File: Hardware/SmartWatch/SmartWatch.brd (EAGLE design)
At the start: 36.8 x 40.6 mm, 70 parts, among them U1 STM32L476, U3 UG-2828GDEDF11, U4 FAN5331SX, U5 APDS-9960, U6 MCP73831, U7 AP2112K-3.3TRG-1

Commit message: finished schematic!
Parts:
- added R19, R22: 10k, resistor:R0603
- added R21: 10K, resistor:R0603
- moved U$41 18.3 mm to (11.5, 10.5), turned to 90 degrees
- moved C19 18.0 mm to (12.0, 8.00), turned to 0 degrees
- moved C18 17.5 mm to (25.0, 7.00), turned to 0 degrees
- moved U$39 16.7 mm to (25.0, 8.50), turned to 0 degrees
- moved U$5 4.92 mm to (9.50, 32.0)
- moved RN1 0.50 mm to (7.00, 20.5)
- moved U1 0.50 mm to (19.5, 14.5), turned to 135 degrees
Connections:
- removed net BT_IRQ: U2.8
- removed net MOSI/DATA1: U3.P$13
- removed net PA10: U1.43
- removed net PA13: U1.46
- removed net PA5: U1.21
- removed net PA6: U1.22
- removed net PA7: U1.23
- removed net PA8: U1.41
- removed net PB0: U1.26
- removed net PB1: U1.27
- removed net PB13: U1.34
- removed net PB14: U1.35
- removed net PB2: U1.28
- removed net PB8: U1.61
- removed net PB9: U1.62
- removed net PC10: U1.51
- removed net PC12: U1.53
- removed net PC4: U1.24
- removed net PC8: U1.39
- removed net PC9: U1.40
- removed net SCK/DATA0: U3.P$14
- new net BT_INT: U1.24, U2.8
- new net OLED_MOSI: U1.53, U3.P$13
- new net OLED_SCK: U1.51, U3.P$14
- net 3.3V: now also R21.2
- net BTN_BACK: now also U1.43
- net BTN_DN: now also U1.26
- net BTN_SEL: now also U1.27
- net BTN_UP: now also U1.28
- net BT_MISO: now also U1.22
- net BT_MOSI: now also U1.23
- net BT_SCK: now also U1.21
- net GND: now also R19.1, R22.1
- net G_INT: now also U1.39
- net IMU_INT: now also U1.40
- net IMU_NRESET: now also R22.2, U1.41
- net OLED_CS: now also R19.2
- net OLED_DC: now also U1.62
- net OLED_RES: now also U1.61
- net SCL: now also U1.34
- net SDA: now also U1.35
- net STAT: now also R21.1, U1.46
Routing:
- added copper zone on layer 1, net GND

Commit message: started board layout
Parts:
- added JP1: (no value), SparkFun-Connectors:1X02
- C1, C10, C11, C14, C2, C3, C4, C5, C6, C7, C8, C9: device microbuilder:0603-MINI -> resistor:C0603
- moved R2 47.7 mm to (18.0, 8.63), flipped to the bottom
- moved R21 46.1 mm to (3.67, 32.0), turned to 180 degrees
- moved R5 46.0 mm to (22.9, 8.89), flipped to the bottom
- moved C3 42.4 mm to (24.1, 8.89), flipped to the bottom
- moved C25 42.2 mm to (11.0, 17.1), turned to 135 degrees
- moved C28 40.0 mm to (11.9, 18.0), turned to 135 degrees
- moved C6 39.3 mm to (25.4, 8.89), flipped to the bottom, turned to 90 degrees
- moved R4 37.8 mm to (15.3, 8.63), flipped to the bottom
- moved C14 37.3 mm to (13.5, 8.68), flipped to the bottom
- moved D2 36.7 mm to (6.45, 29.3), flipped to the bottom
- moved C9 36.6 mm to (12.3, 8.68), flipped to the bottom
- moved C27 35.0 mm to (21.0, 24.1), turned to 90 degrees
- moved D3 33.9 mm to (21.4, 12.5), flipped to the bottom, turned to 90 degrees
- moved D1 33.5 mm to (23.1, 12.5), flipped to the bottom
- moved L1 29.1 mm to (7.08, 34.0), flipped to the bottom, turned to 270 degrees
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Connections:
- removed net 3.3V: BTN_BACK.3, BTN_BACK.4, BTN_BOOT0.3, BTN_BOOT0.4, BTN_DN.3, BTN_DN.4, BTN_NRST.3, BTN_NRST.4, BTN_SEL.3, BTN_SEL.4, BTN_UP.3, BTN_UP.4, C10.2, C11.2, C12.1, C13.1, C18.1, C19.1, C20.1, C21.1, C22.1, C23.1, C24.1, C25.1, C26.1, C29.1, C3.2, C5.2, C7.1, C9.2, L1.P$1, R21.2, R3.2, R8.2, R9.2, U$39.4, U$41.4, U$5.28, U$5.3, U$5.4, U1.1, U1.13, U1.19, U1.32, U1.48, U1.64, U3.P$27, U3.P$4, U4.4, U4.5, U5.5, U5.8, U7.5
- net +3V3: now also BTN_BACK.3, BTN_BACK.4, BTN_BOOT0.3, BTN_BOOT0.4, BTN_DN.3, BTN_DN.4, BTN_NRST.3, BTN_NRST.4, BTN_SEL.3, BTN_SEL.4, BTN_UP.3, BTN_UP.4, C10.2, C11.2, C12.1, C13.1, C18.1, C19.1, C20.1, C21.1, C22.1, C23.1, C24.1, C25.1, C26.1, C29.1, C3.2, C5.2, C7.1, C9.2, L1.P$1, R21.2, R3.2, R8.2, R9.2, U$39.4, U$41.4, U$5.28, U$5.3, U$5.4, U1.1, U1.13, U1.19, U1.32, U1.48, U1.64, U3.P$27, U3.P$4, U4.4, U4.5, U5.5, U5.8, U7.5
- net GND: now also JP1.1
- net VBAT: now also JP1.2
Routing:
- net +3V3: track 0.00 -> 35.0 mm
- net BTN_UP: track 0.00 -> 34.6 mm, vias 0 -> 1
- net BTN_NRST: track 0.00 -> 30.0 mm, vias 0 -> 1
- net BTN_DN: track 0.00 -> 29.5 mm, vias 0 -> 1
- net BTN_SEL: track 0.00 -> 21.3 mm, vias 0 -> 1
- net VUSB: track 0.00 -> 21.0 mm, vias 0 -> 1
- net BT_SCK: track 0.00 -> 17.2 mm, vias 0 -> 2
- net BT_MISO: track 0.00 -> 15.1 mm, vias 0 -> 2
- net D-: track 0.00 -> 13.6 mm, vias 0 -> 1
- net BT_MOSI: track 0.00 -> 13.1 mm, vias 0 -> 2
- net OLED_SCK: track 0.00 -> 12.2 mm, vias 0 -> 1
- net OLED_MOSI: track 0.00 -> 12.1 mm, vias 0 -> 1
- net VBAT: track 0.00 -> 11.3 mm
- net D+: track 0.00 -> 11.2 mm, vias 0 -> 1
- net BT_INT: track 0.00 -> 10.4 mm, vias 0 -> 2
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- added copper zone on layer 16, net GND

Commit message: finished PCB and added images
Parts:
- moved C2 41.1 mm to (26.7, 8.91), flipped to the bottom
- moved U4 41.0 mm to (33.3, 14.4)
- moved R6 38.8 mm to (34.6, 10.9), turned to 270 degrees
- moved R7 38.7 mm to (32.0, 10.9)
- moved C8 38.6 mm to (33.3, 10.9)
- moved C12 32.4 mm to (13.8, 34.0)
- moved C1 32.3 mm to (21.1, 31.8), turned to 270 degrees
- moved C7 31.7 mm to (28.3, 17.3), turned to 45 degrees
- moved D2 30.7 mm to (30.0, 9.60), flipped to the top
- moved R3 30.4 mm to (17.5, 24.0), turned to 0 degrees
- moved L1 30.1 mm to (30.0, 14.4), flipped to the top
- moved C4 28.9 mm to (10.6, 23.6), turned to 90 degrees
- moved R8 26.3 mm to (17.5, 22.8), turned to 0 degrees
- moved C5 25.3 mm to (7.83, 28.5), turned to 0 degrees
- moved R11 23.2 mm to (7.90, 25.8), turned to 0 degrees
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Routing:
- net +3V3: track 35.0 -> 263.1 mm, vias 0 -> 7
- net SDA: track 0.00 -> 30.2 mm, vias 0 -> 3
- net G_INT: track 0.00 -> 27.4 mm, vias 0 -> 2
- net STAT: track 3.87 -> 30.0 mm
- net BTN_BACK: track 4.94 -> 28.9 mm, vias 0 -> 1
- net SCL: track 0.00 -> 22.5 mm, vias 0 -> 2
- net BTN_BOOT0: track 4.98 -> 20.6 mm, vias 0 -> 1
- net 13V: track 0.00 -> 13.1 mm, vias 0 -> 1
- net IMU_NRESET: track 0.00 -> 9.75 mm
- net IMU_INT: track 0.00 -> 9.18 mm
- net N$5: track 0.00 -> 4.30 mm
- net N$8: track 0.00 -> 4.06 mm
- net N$4: track 0.00 -> 2.99 mm
- net VBAT: track 11.3 -> 13.9 mm
- net N$14: track 0.00 -> 2.11 mm
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- added copper zone on layer 1, net VUSB

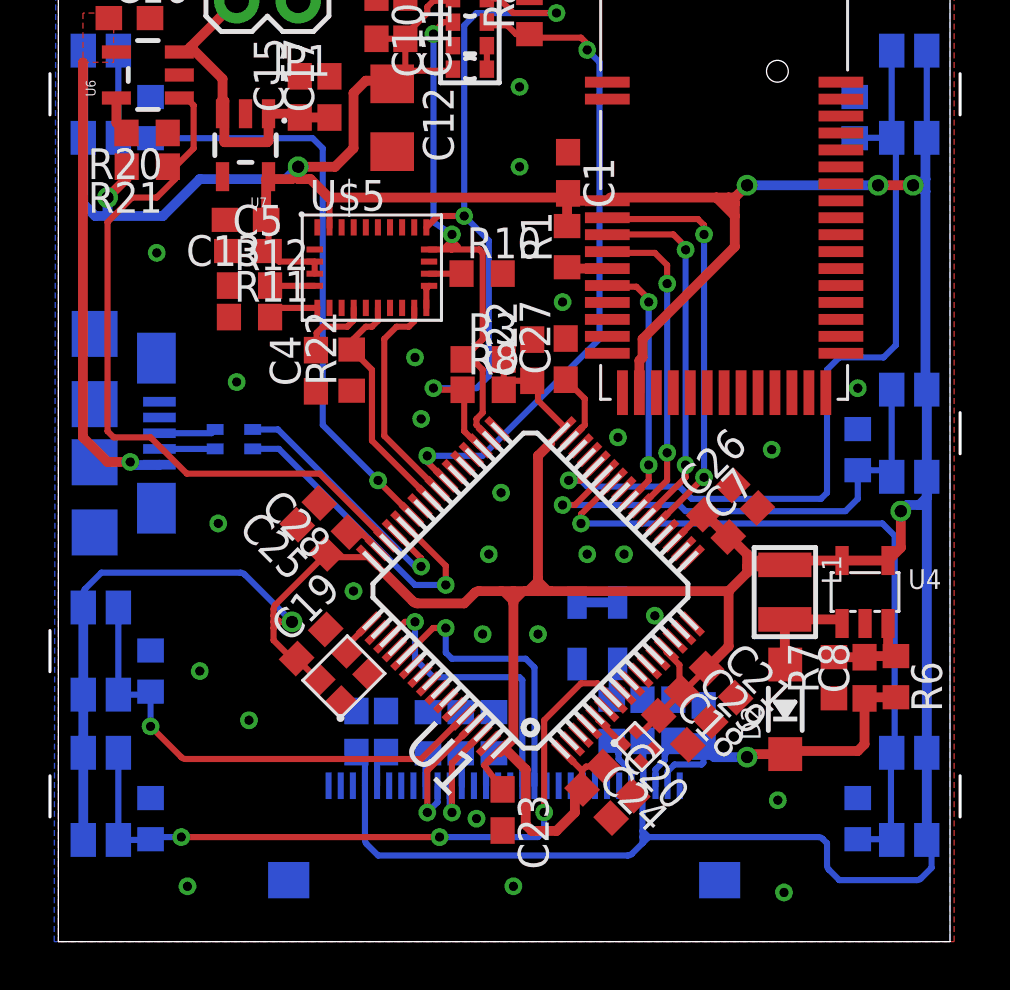
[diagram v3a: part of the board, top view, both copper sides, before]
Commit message: updated with ext programming port also eliminated some gnd loops and added text
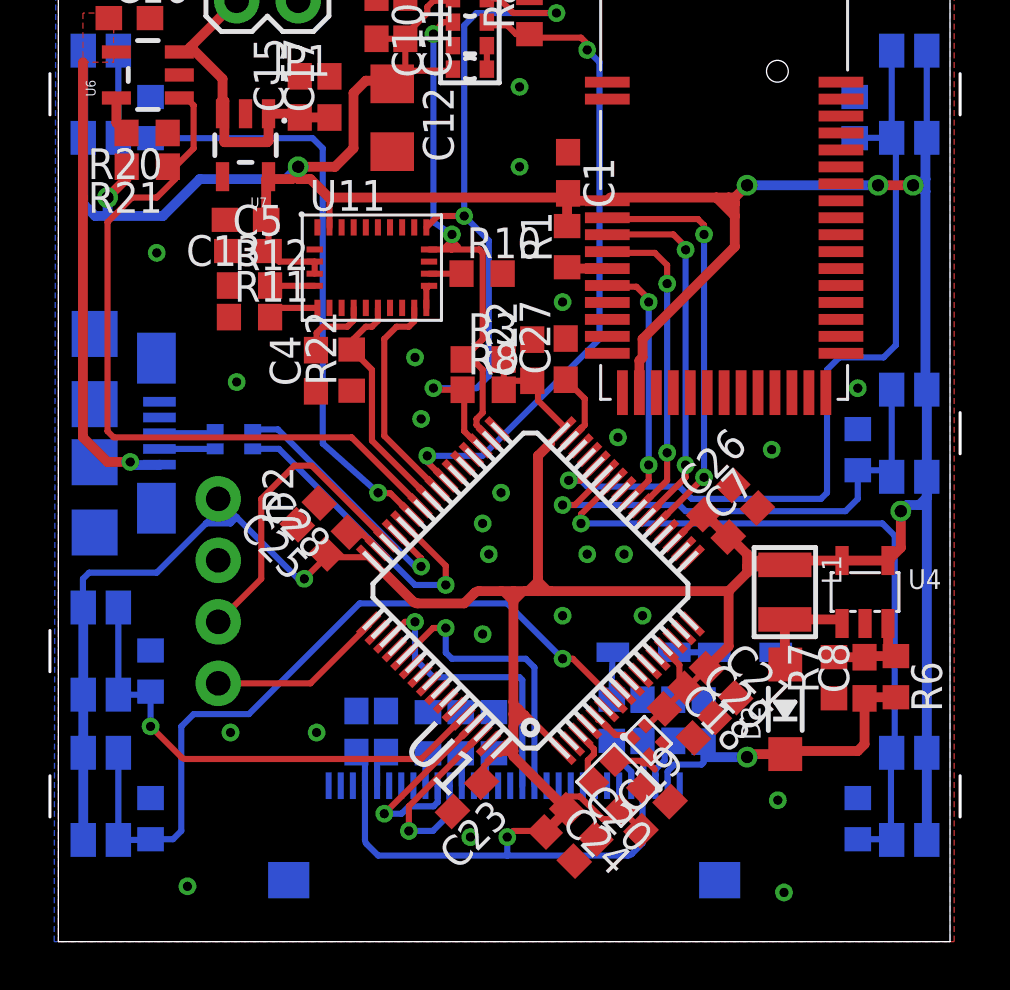
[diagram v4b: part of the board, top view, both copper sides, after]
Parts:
- removed U$39: ASCO-8, SmartWatch:ASCO-8
- removed U$41: ASDK-32.768, SmartWatch:ASDK-32.768
- added JP2: (no value), SparkFun-Connectors:1X04_NO_SILK_ALL_ROUND
- added U8: ASDK-32.768, SmartWatch:ASDK-32.768
- added U9: ASCO-8, SmartWatch:ASCO-8
- C10: value 1.0uF -> 1uF
- C2, C6: value 10uF/16V -> 10uF
- C22: value 0.1nF -> 0.1uF
- R13, R14, R15, R16, R17, R18, R20, R21, R7, R9: value 10K -> 10k
- R4: value 600K -> 600k
- R6: value 100K -> 100k
- RN1: value (none) -> 22
- moved C19 15.9 mm to (24.7, 5.18)
- moved D3 6.98 mm to (28.4, 11.9), turned to 0 degrees
- moved C24 2.34 mm to (20.7, 3.93)
- moved C20 2.34 mm to (21.6, 4.85)
- moved C23 1.56 mm to (16.9, 5.98), turned to 225 degrees
- moved D1 1.33 mm to (24.2, 12.0), turned to 0 degrees
- moved C18 0.36 mm to (25.6, 9.01)
- moved C29 0.22 mm to (26.5, 9.86)
- moved C2 0.20 mm to (26.7, 9.11)
- renumbered U$16 to U10, U$5 to U11
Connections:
- removed net PA9: U1.42
- removed net PC14: U1.3
- new net SWCLK: JP2.4, U1.49
- new net SWDIO: JP2.3, U1.46
- net +3V3: now also JP2.1, U8.4, U9.4; no longer U$39.4, U$41.4
- net GND: now also JP2.2, U8.2, U9.2; no longer U$39.2, U$41.2
- net OSC32_IN: now also U1.3, U8.3; no longer U$41.3, U1.49
- net OSC_IN: now also U9.1; no longer U$39.1
- net STAT: now also U1.42; no longer U1.46
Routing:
- net SWDIO: track 0.00 -> 12.8 mm
- net +3V3: track 263.1 -> 253.2 mm, vias 7 -> 8
- net SWCLK: track 0.00 -> 7.26 mm
- net OLED_DC: track 4.81 -> 8.32 mm
- net BTN_NRST: track 29.8 -> 32.4 mm, vias 3 -> 1
- net OLED_RES: track 5.58 -> 8.17 mm
- net GND: track 1.57 -> 3.74 mm, vias 26 -> 24
- net STAT: track 30.0 -> 30.9 mm
- net OSC32_IN: track 1.55 -> 2.34 mm
- net 13V: track 13.1 -> 13.6 mm
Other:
- board text added: "ECE 477 Group 4 Designed by Nick Molo"

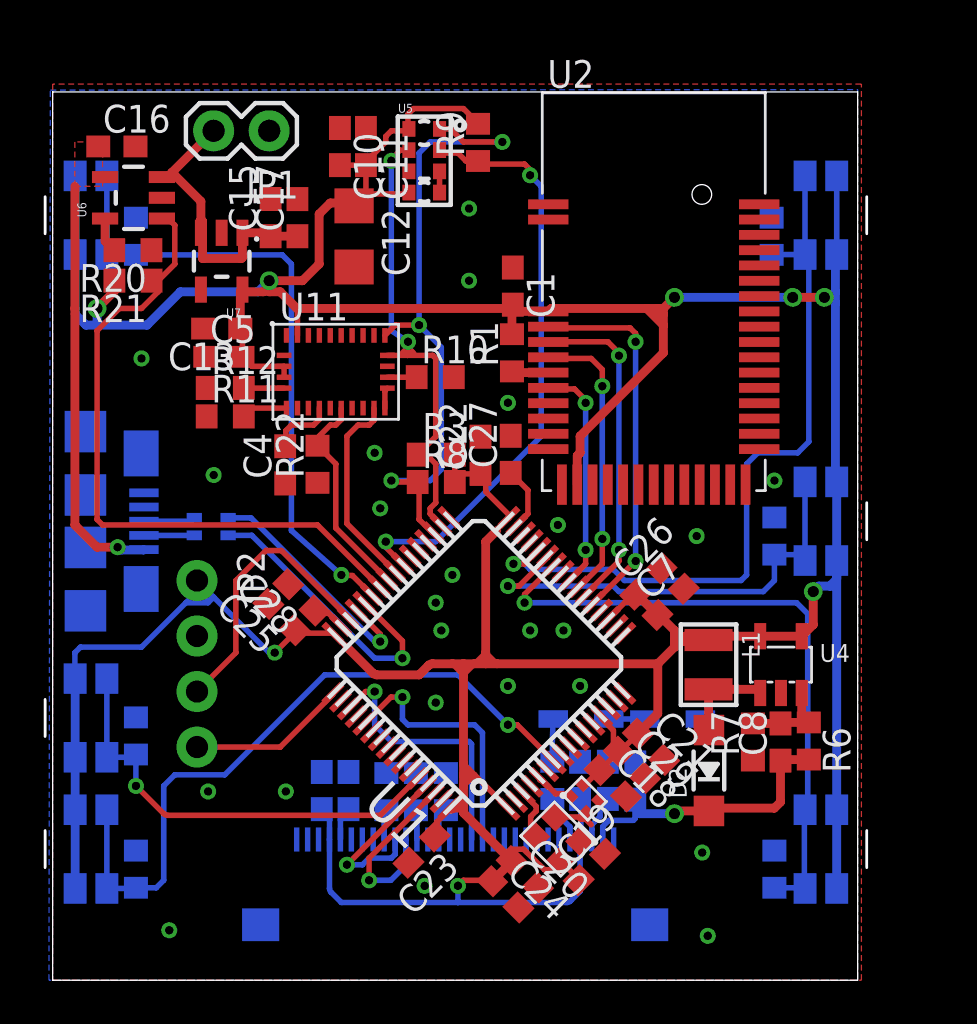
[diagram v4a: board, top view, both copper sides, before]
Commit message: added mounting holes
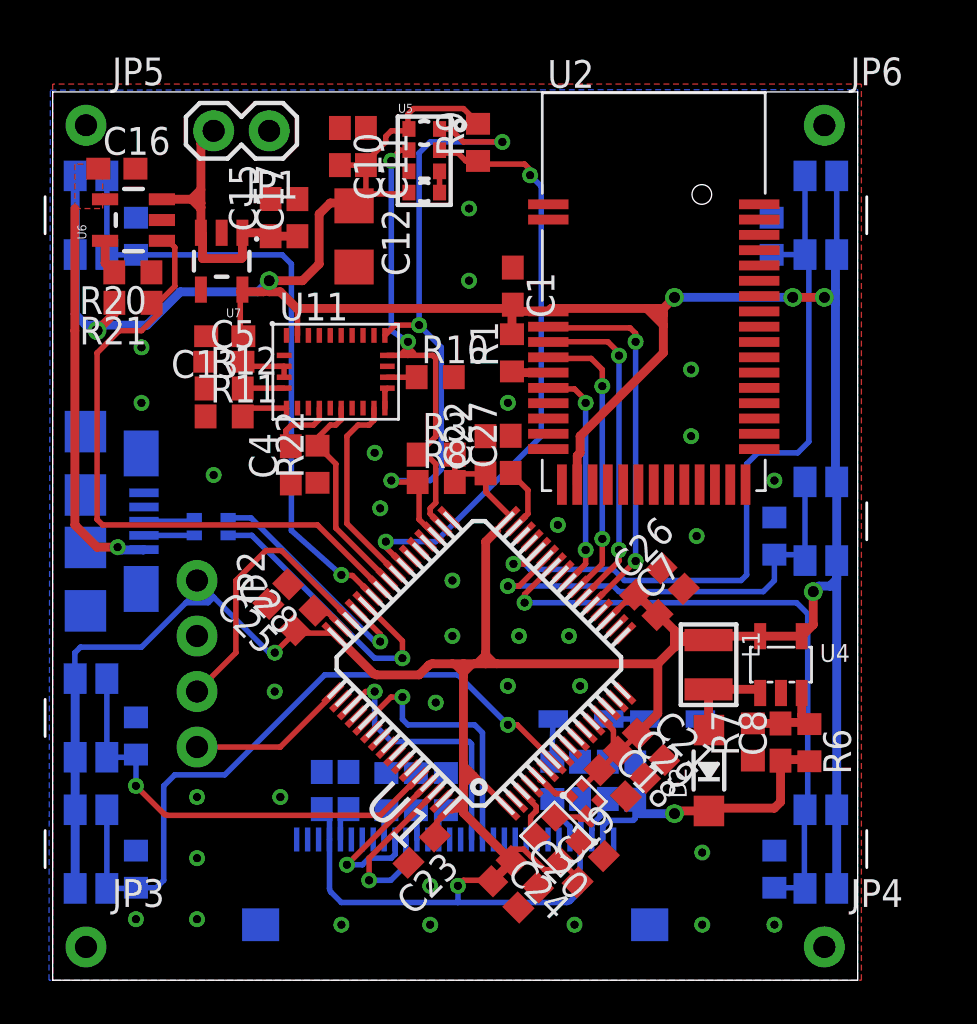
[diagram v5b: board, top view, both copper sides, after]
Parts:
- added JP3, JP4, JP5, JP6: (no value), SparkFun-Connectors:1X01_NO_SILK
- moved R21 1.02 mm to (3.67, 31.0)
- moved C16 1.02 mm to (2.94, 37.1)
- moved R20 1.02 mm to (3.67, 32.4)
- moved U6 1.02 mm to (3.70, 34.8)
- moved C13 0.38 mm to (7.87, 29.5)
- moved C4 0.25 mm to (10.9, 23.6)
- moved C22 0.23 mm to (19.8, 24.0)
- moved C5 0.23 mm to (7.83, 28.3)
- moved C19 0.11 mm to (24.6, 5.08)
- moved R6 0.08 mm to (34.6, 10.9)
- moved R12 0.06 mm to (7.85, 27.1)
- moved R11 0.05 mm to (7.85, 25.8)
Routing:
- net VUSB: track 19.2 -> 18.2 mm
- net STAT: track 30.9 -> 29.8 mm
- net VBAT: track 13.9 -> 14.7 mm
- net GND: vias 24 -> 33

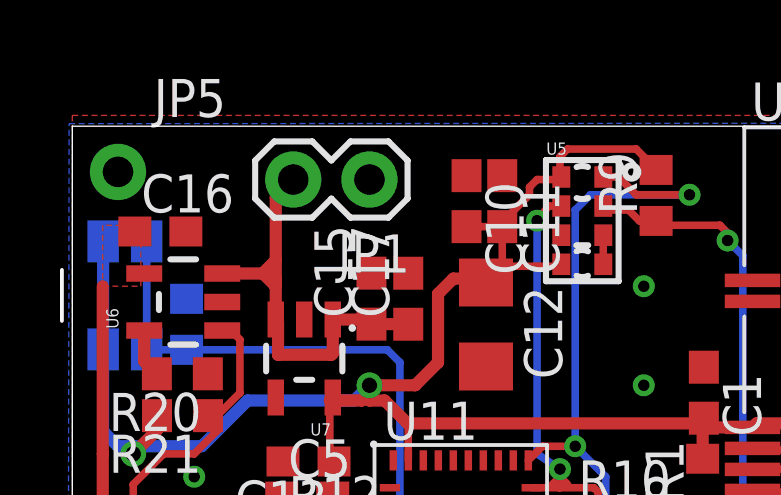
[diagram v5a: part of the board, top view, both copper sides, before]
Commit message: changed mounting holes to pin headers
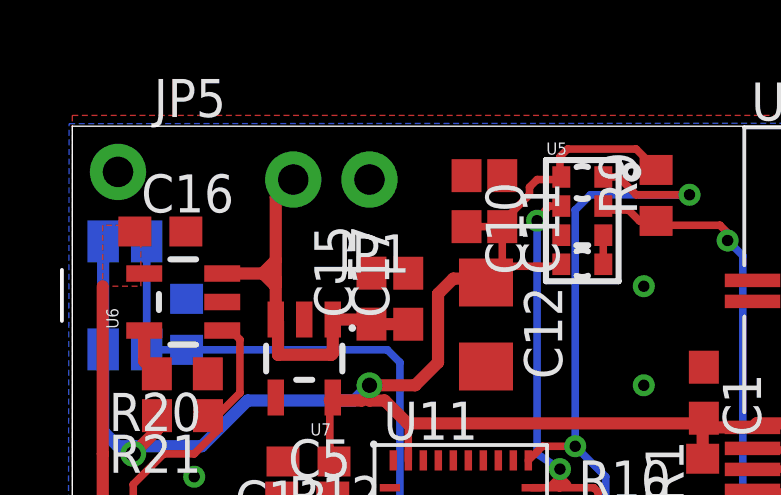
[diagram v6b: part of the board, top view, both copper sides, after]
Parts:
- JP1: device SparkFun-Connectors:1X02 -> SparkFun-Connectors:1X02_NO_SILK
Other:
- board text added: "+"
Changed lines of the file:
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@@
 <setting verticaltext="up"/>
 </settings>
-<grid distance="0.01" unitdist="inch" unit="inch" style="lines" multiple="1" display="yes" altdistance="0.001" altunitdist="inch" altunit="inch"/>
+<grid distance="0.05" unitdist="inch" unit="inch" style="lines" multiple="1" display="yes" altdistance="0.005" altunitdist="inch" altunit="inch"/>
 <layers>
 <layer number="1" name="Top" color="4" fill="1" visible="yes" active="yes"/>
@@
 <layer number="50" name="dxf" color="7" fill="1" visible="no" active="no"/>
 <layer number="51" name="tDocu" color="6" fill="1" visible="yes" active="yes"/>
-<layer number="52" name="bDocu" color="7" fill="1" visible="no" active="yes"/>
+<layer number="52" name="bDocu" color="7" fill="1" visible="yes" active="yes"/>
 <layer number="53" name="tGND_GNDA" color="7" fill="1" visible="no" active="no"/>
 <layer number="54" name="bGND_GNDA" color="7" fill="1" visible="no" active="no"/>
@@
 Designed by
 Nick Molo</text>
+<text x="4.826" y="38.1" size="1.778" layer="51" font="vector" ratio="15">+</text>
 </plain>
 <attributes>
@@
 <element name="R21" library="resistor" package="R0603" value="10k" x="3.6736" y="30.9926" rot="R180"/>
 <element name="R22" library="resistor" package="R0603" value="10k" x="12.1166" y="23.606" rot="R90"/>
-<element name="JP1" library="SparkFun-Connectors" package="1X02" value="" x="9.906" y="38.862" rot="R180"/>
+<element name="JP1" library="SparkFun-Connectors" package="1X02_NO_SILK" value="" x="9.906" y="38.862" rot="R180"/>
 <element name="JP2" library="SparkFun-Connectors" package="1X04_NO_SILK_ALL_ROUND" value="" x="6.604" y="18.288" rot="R270"/>
 <element name="JP3" library="SparkFun-Connectors" package="1X01_NO_SILK" value="" x="1.524" y="1.524"/>

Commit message: update board
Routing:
- net GND: vias 33 -> 34
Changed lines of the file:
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@@
 <layer number="50" name="dxf" color="7" fill="1" visible="no" active="no"/>
 <layer number="51" name="tDocu" color="6" fill="1" visible="yes" active="yes"/>
-<layer number="52" name="bDocu" color="7" fill="1" visible="yes" active="yes"/>
+<layer number="52" name="bDocu" color="7" fill="1" visible="no" active="yes"/>
 <layer number="53" name="tGND_GNDA" color="7" fill="1" visible="no" active="no"/>
 <layer number="54" name="bGND_GNDA" color="7" fill="1" visible="no" active="no"/>
@@
 <vertex x="0" y="0"/>
 <vertex x="37" y="0"/>
-<vertex x="37" y="41"/>
-<vertex x="0" y="41"/>
+<vertex x="36.8222" y="40.6444"/>
+<vertex x="32.7704" y="40.6444"/>
+<vertex x="32.766" y="37.084"/>
+<vertex x="22.352" y="37.084"/>
+<vertex x="22.352" y="40.64"/>
+<vertex x="-0.0254" y="40.6444"/>
 </polygon>
 <contactref element="R22" pad="1"/>
@@
 <vertex x="-0.17" y="0"/>
 <vertex x="-0.106" y="40.724"/>
+<vertex x="22.352" y="40.64"/>
+<vertex x="22.352" y="37.084"/>
+<vertex x="32.766" y="37.084"/>
+<vertex x="32.7704" y="40.6444"/>
 <vertex x="36.83" y="40.746"/>
 </polygon>
@@
 <via x="29.21" y="27.94" extent="1-16" drill="0.381"/>
 <via x="4.064" y="26.416" extent="1-16" drill="0.381"/>
+<via x="21.59" y="39.37" extent="1-16" drill="0.381"/>
 <wire x1="24.273484375" y1="7.46793125" x2="24.384" y2="7.366" width="0" layer="19" extent="1-1"/>
 </signal>
